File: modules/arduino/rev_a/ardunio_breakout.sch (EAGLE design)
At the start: 2 parts, among them J1 MODULE_GENERIC, U1 ARDUINO_SHIELDLABEL

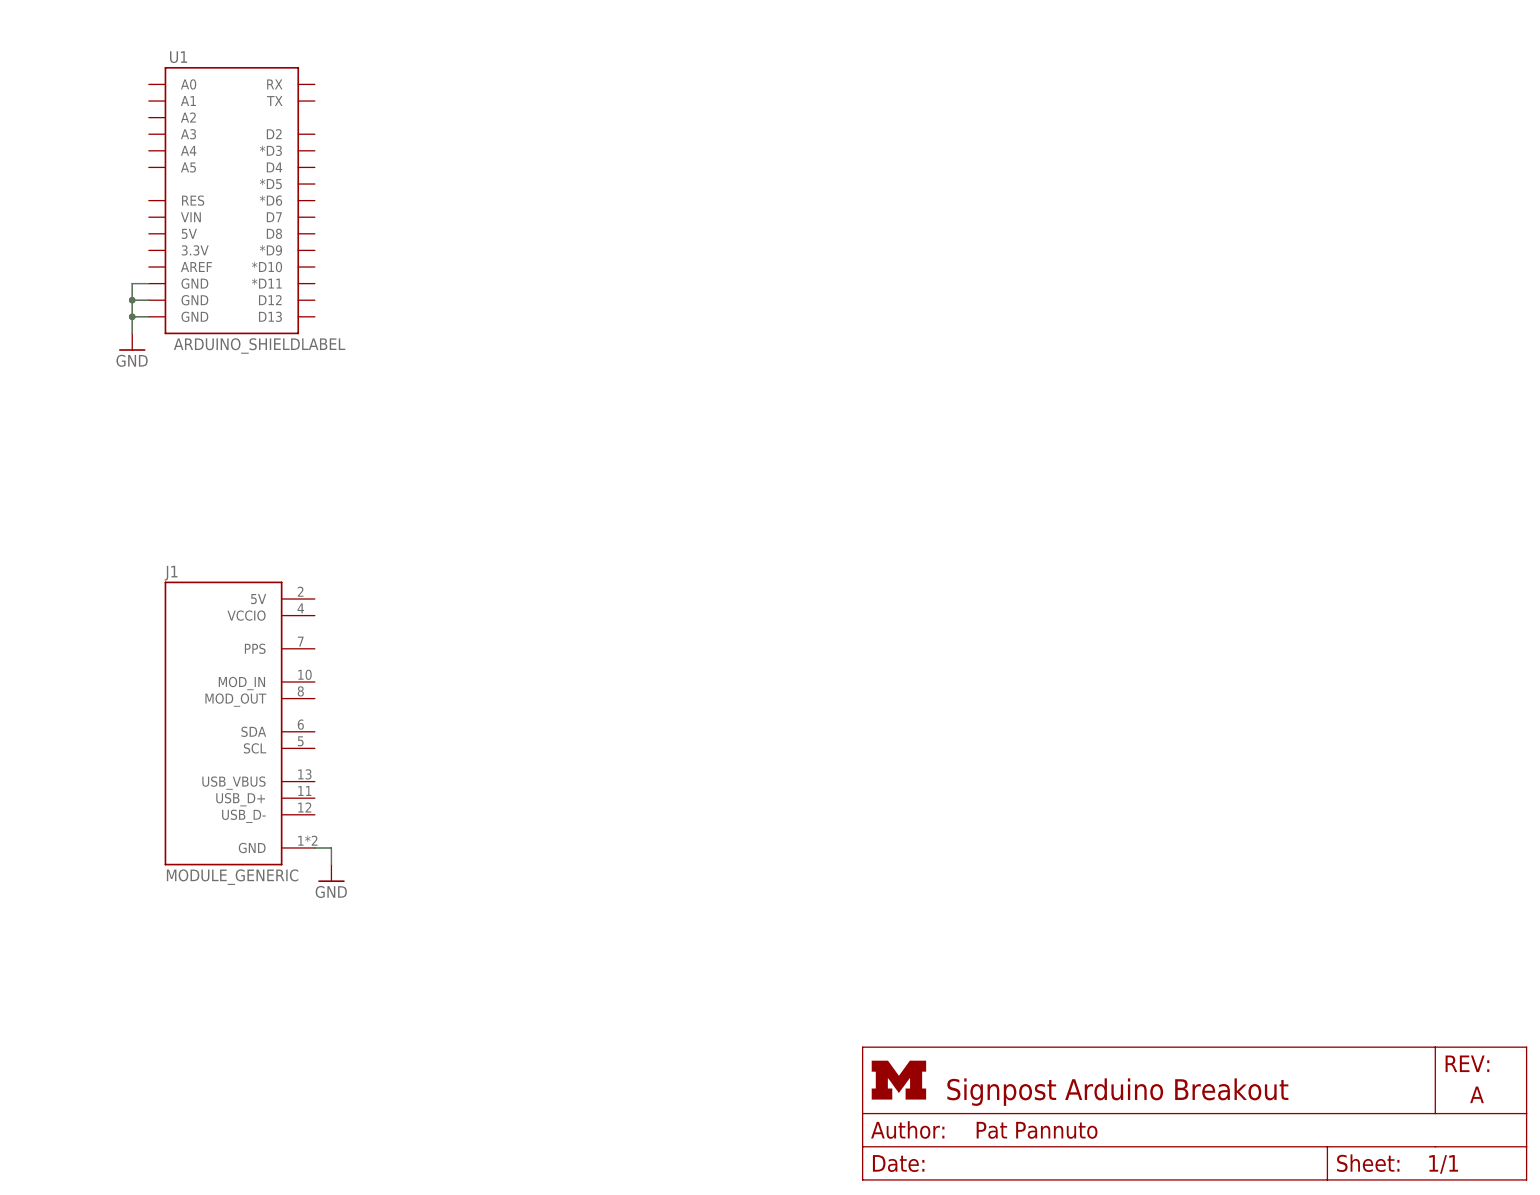
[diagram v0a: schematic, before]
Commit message: Arduino Module: Regulator and headers
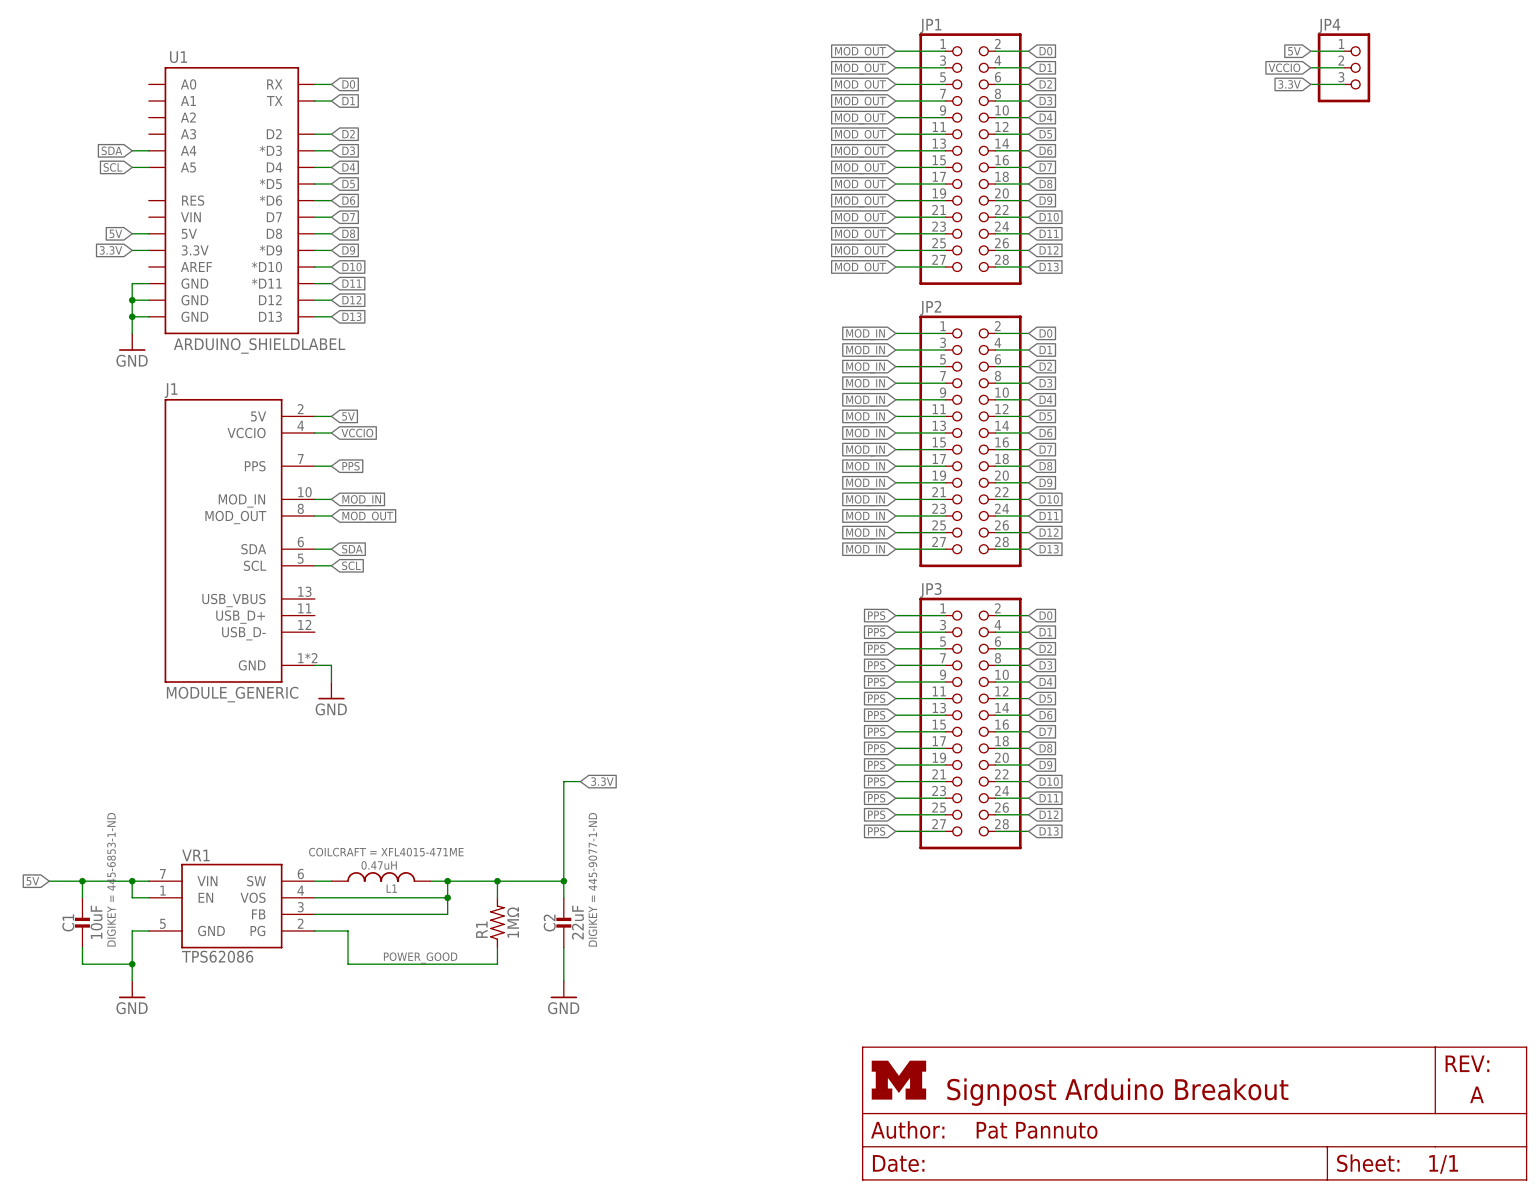
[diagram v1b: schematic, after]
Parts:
- added C1: 10uF, passives:CAPACITOR0603_CAP
- added C2: 22uF, passives:CAPACITOR0603_CAP
- added JP1, JP2, JP3: (no value), pinhead:PINHD-2X14
- added JP4: (no value), pinhead:PINHD-1X3
- added L1: 0.47uH, passives:INDUCTORXFL4015
- added R1: 1MΩ, passives:RESISTOR0603_RES
- added VR1: TPS62086, regulators:TPS62086
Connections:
- new net 3.3V: C2.1, JP4.3, L1.2, R1.2, U1.3.3V, VR1.FB, VR1.VOS
- new net 5V: C1.1, J1.5V, JP4.1, U1.5V, VR1.EN, VR1.VIN
- new net D0: JP1.2, JP2.2, JP3.2, U1.RX
- new net D1: JP1.4, JP2.4, JP3.4, U1.TX
- new net D10: JP1.22, JP2.22, JP3.22, U1.*D10
- new net D11: JP1.24, JP2.24, JP3.24, U1.*D11
- new net D12: JP1.26, JP2.26, JP3.26, U1.D12
- new net D13: JP1.28, JP2.28, JP3.28, U1.D13
- new net D2: JP1.6, JP2.6, JP3.6, U1.D2
- new net D3: JP1.8, JP2.8, JP3.8, U1.*D3
- new net D4: JP1.10, JP2.10, JP3.10, U1.D4
- new net D5: JP1.12, JP2.12, JP3.12, U1.*D5
- new net D6: JP1.14, JP2.14, JP3.14, U1.*D6
- new net D7: JP1.16, JP2.16, JP3.16, U1.D7
- new net D8: JP1.18, JP2.18, JP3.18, U1.D8
- new net D9: JP1.20, JP2.20, JP3.20, U1.*D9
- new net MOD_IN: J1.MOD_IN, JP2.1
- new net MOD_OUT: J1.MOD_OUT, JP1.1, JP1.11, JP1.13, JP1.15, JP1.17, JP1.19, JP1.21, JP1.23, JP1.25, JP1.27, JP1.3, JP1.5, JP1.7, JP1.9
- new net N$1: L1.1, VR1.SW
- new net POWER_GOOD: R1.1, VR1.PG
- new net PPS: J1.PPS, JP3.1
- new net SCL: J1.SCL, U1.A5
- new net SDA: J1.SDA, U1.A4
- new net VCCIO: J1.VCCIO, JP4.2
- net GND: now also C1.2, C2.2, VR1.GND
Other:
- note added: "Pins 0, 1 are UART"
- note added: "Pins 10, 11, 12, 13 are SPI"
- note added: "Pins 2, 3 have interrupt support"
- note added: "Pins 3, 5, 6, 9, 10, 11 have PWM support"
- note added: "Pins 4, 10, 11, 12, 13 are reserved on Arduino Ethernet, so some shields may avoid using them"
- moved on the sheet: J1
